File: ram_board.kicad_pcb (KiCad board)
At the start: 2 copper layers, 73 x 31.6 mm, 20 parts, among them J1 Conn_02x20_Odd_Even, J2 Conn_02x05_Odd_Even, U1 IS61LV5128AL-10TLI, U2 SST39VF040-70-4C-NHE, U3 74LVC04A

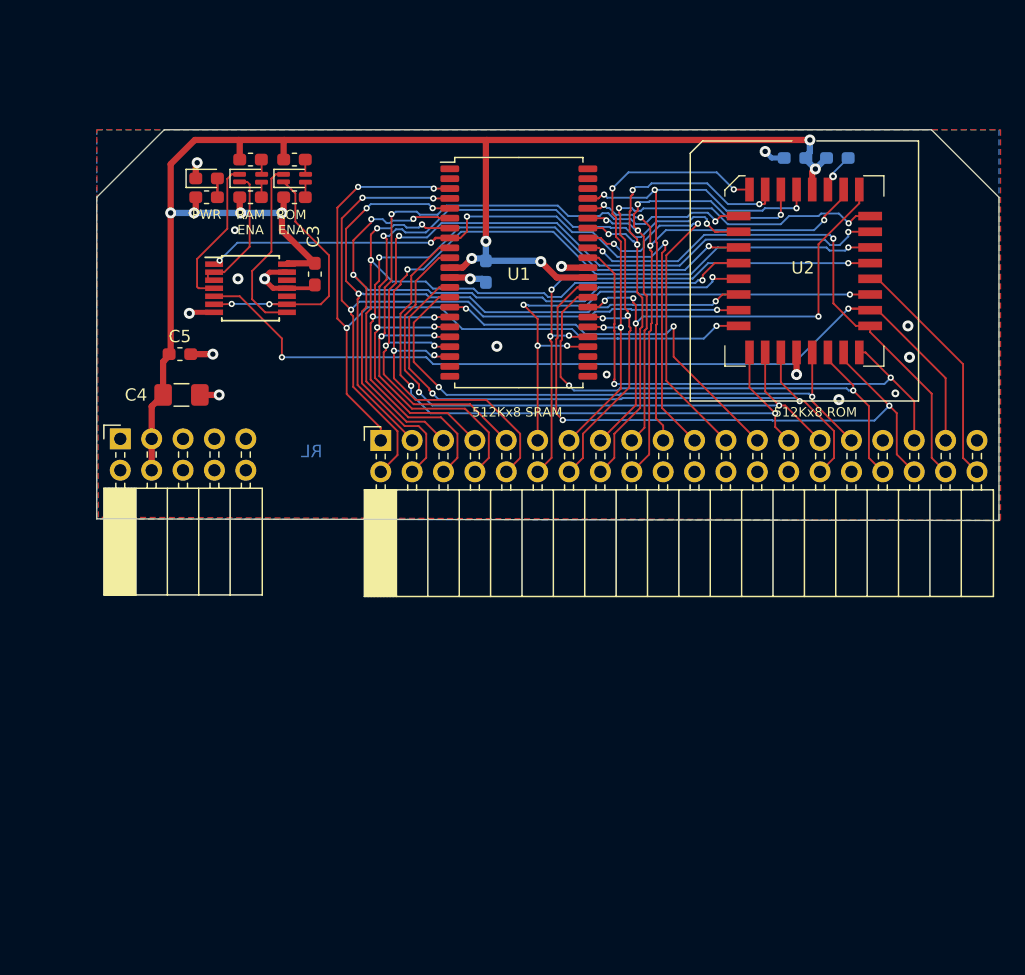
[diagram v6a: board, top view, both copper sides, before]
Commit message: fixed leds, spacing
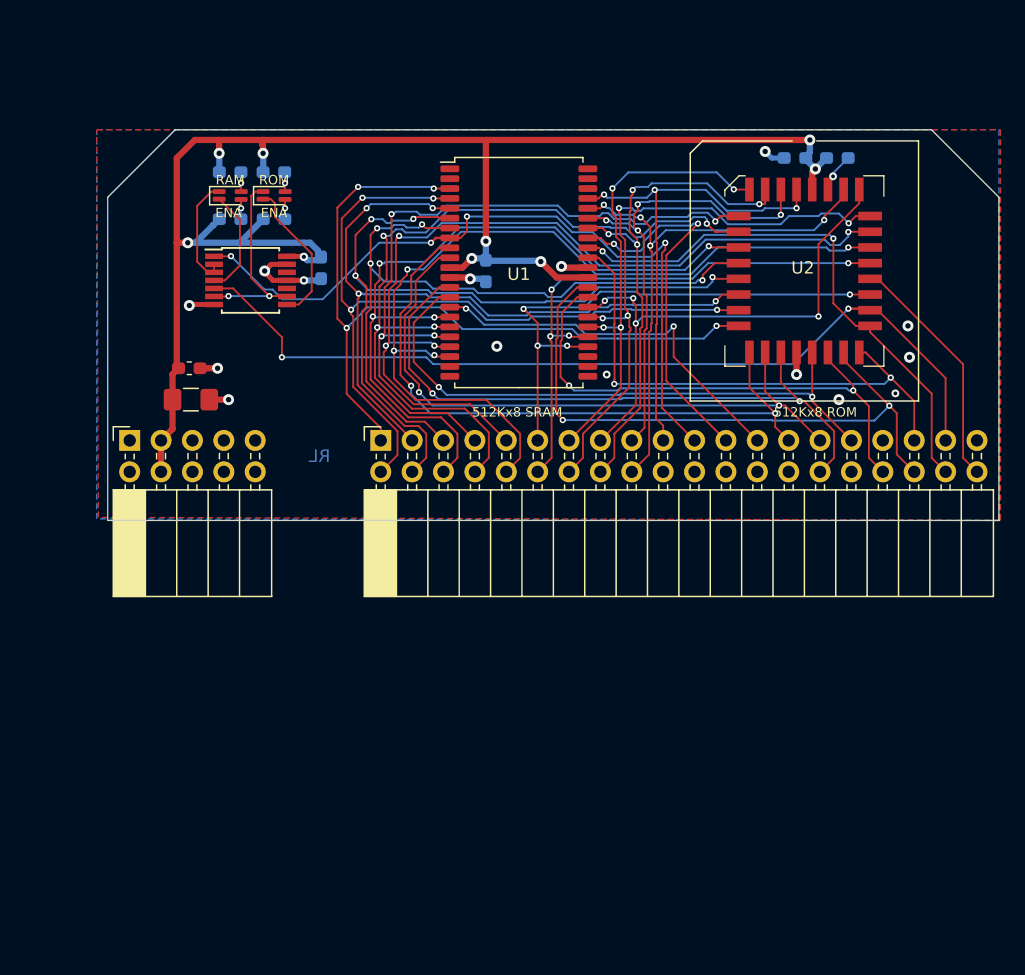
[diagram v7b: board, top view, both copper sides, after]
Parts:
- removed D1: LED, LED_SMD:LED_0603_1608Metric_Pad1.05x0.95mm_HandSolder
- removed R1: 360R, Resistor_SMD:R_0603_1608Metric_Pad1.05x0.95mm_HandSolder
- C3, R3, R4, R5, R6: moved to B.Cu
- moved G*** 33.7 mm to (167.4, 86.1)
- moved R6 5.10 mm to (131.4, 79.8)
- moved R4 5.10 mm to (127.9, 79.8)
- moved R5 2.63 mm to (131.4, 75.9)
- moved R3 2.62 mm to (127.9, 75.9)
- moved D3 2.16 mm to (131.4, 77.9)
- moved D2 2.16 mm to (127.9, 77.9)
- moved C5 1.37 mm to (124.6, 91.8)
- moved C4 0.85 mm to (124.7, 94.4)
- moved J2 0.77 mm to (119.8, 97.7)
- moved C3 0.72 mm to (135.3, 83.7)
- moved U3 0.63 mm to (129.5, 84.7)
- moved C2 0.05 mm to (148.6, 83.9)
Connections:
- R3 pad 1: Net-(D2-Pad3) -> Net-(D2-Pad1)
- R4 pad 1: Net-(D2-Pad1) -> Net-(D2-Pad3)
- R5 pad 1: Net-(D3-Pad3) -> Net-(D3-Pad1)
- R6 pad 1: Net-(D3-Pad1) -> Net-(D3-Pad3)
- U3 pad 2: Net-(D2-Pad4) -> Net-(D2-Pad2)
- U3 pad 3: Net-(D2-Pad4) -> Net-(D2-Pad2)
- U3 pad 4: Net-(D2-Pad2) -> Net-(D2-Pad4)
- U3 pad 6: Net-(D3-Pad4) -> Net-(D3-Pad2)
- U3 pad 8: Net-(D3-Pad2) -> Net-(D3-Pad4)
- U3 pad 9: Net-(D3-Pad4) -> Net-(D3-Pad2)
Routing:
- net Net-(D3-Pad4): track 22.2 -> 11.9 mm, vias 2 -> 0
- net /RAM_CE: track 58.4 -> 61.2 mm
- net Net-(D2-Pad2): track 11.8 -> 9.15 mm
- net +3V3: track 130.9 -> 133.4 mm
- net Net-(D2-Pad4): track 10.8 -> 8.85 mm
- net Net-(D3-Pad2): track 15.3 -> 17.2 mm, vias 0 -> 2
- net Net-(D1-Pad2): track 1.52 -> 0.00 mm
- net GND: track 23.5 -> 22.0 mm, vias 17 -> 15
- net Net-(D3-Pad1): track 1.20 -> 1.62 mm, vias 0 -> 1
- net Net-(D3-Pad3): track 1.22 -> 1.61 mm, vias 0 -> 1
- net Net-(D2-Pad3): track 1.22 -> 1.61 mm, vias 0 -> 1
- net Net-(D2-Pad1): track 1.20 -> 1.59 mm, vias 0 -> 1
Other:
- board size 73 x 31.6 mm -> 72.1 x 31.6 mm
- board text added: "DeltaBrd RAM/ROM Extension v1.0 © 2019 by Hyiger Designs"
- board text added: "ENA"
- board text added: "RAM"
- board text added: "ROM"
- board text removed: "DeltaBrd RAM/ROM Extension v1.0 © 2019 by Hyiger Designs DeltaBrd © Dr. Svetozar Ilchev http://ilchev.net/deltabrd"
- board text removed: "PWR"
- board text removed: "RAM ENA"
- board text removed: "ROM ENA"

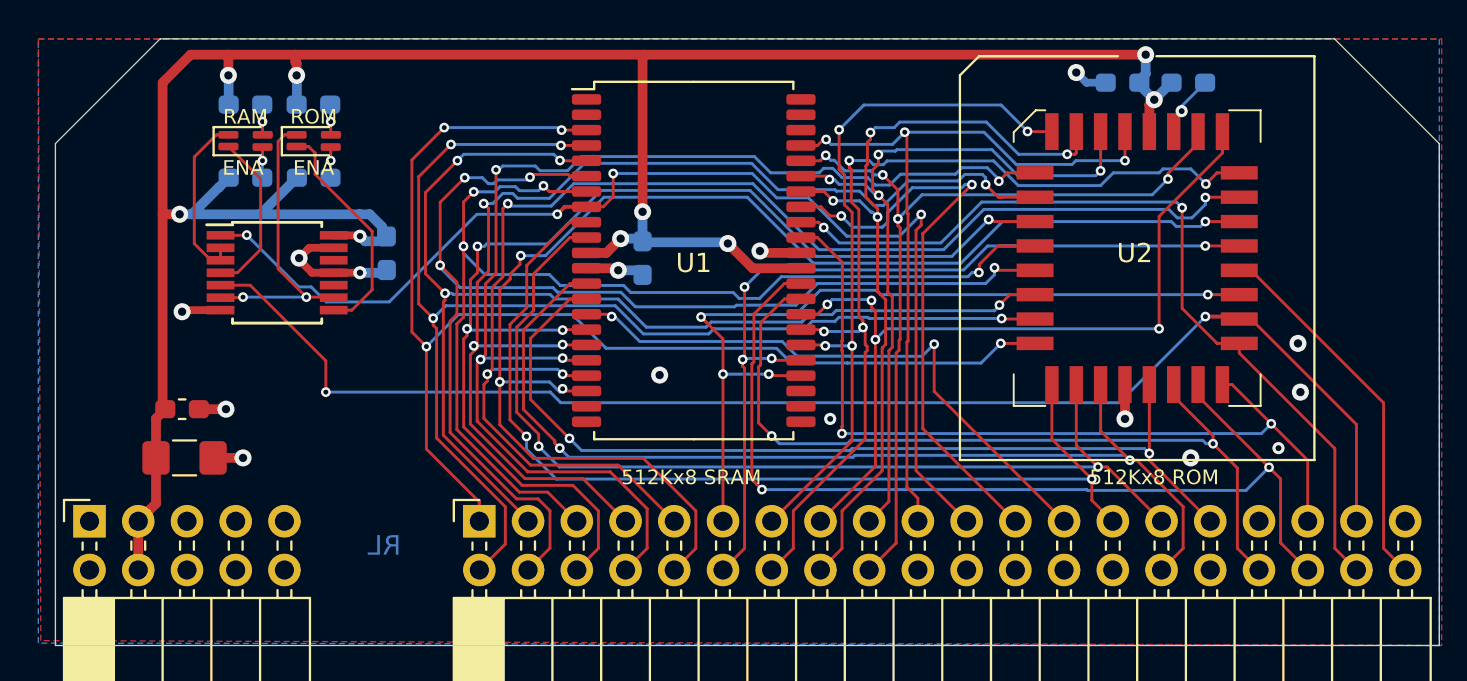
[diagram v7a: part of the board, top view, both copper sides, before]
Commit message: gnd plane stitching
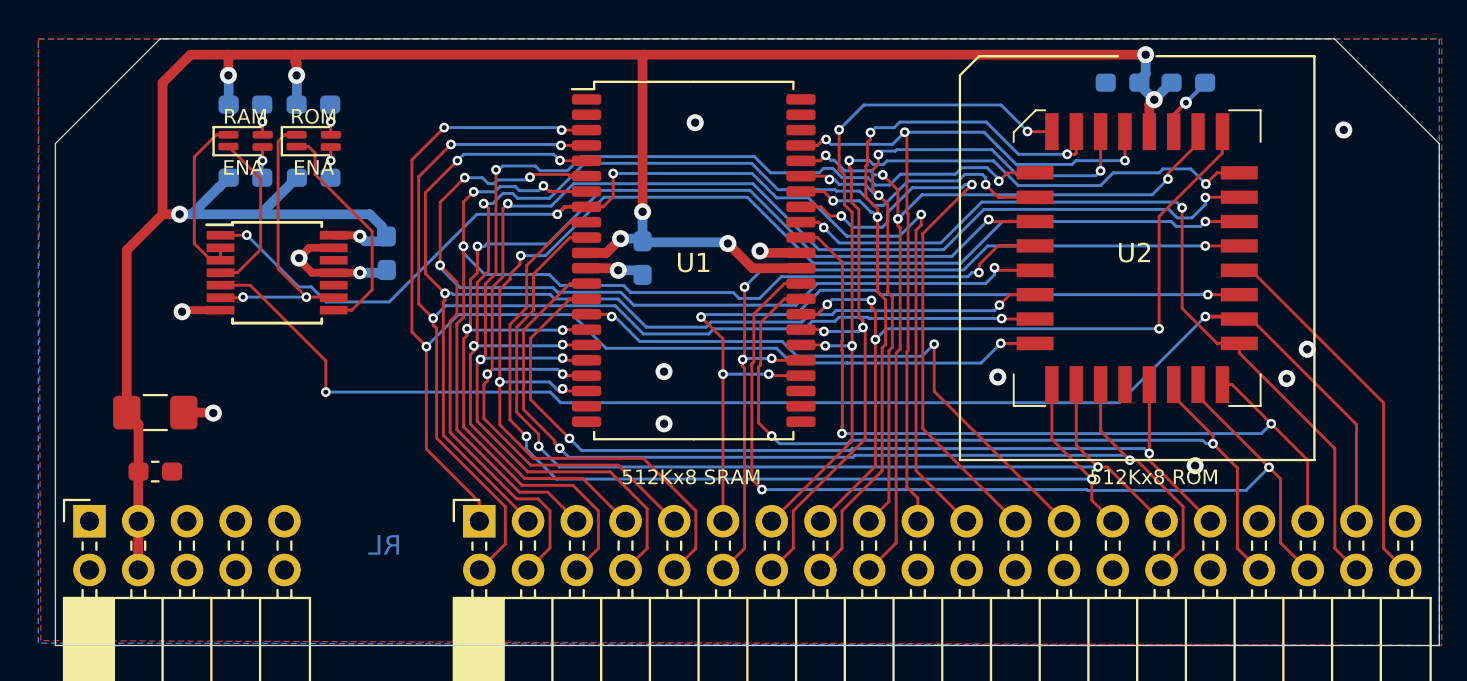
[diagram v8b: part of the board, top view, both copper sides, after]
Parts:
- moved C5 3.54 mm to (123.2, 95.1)
- moved C4 2.81 mm to (123.2, 92.0)
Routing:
- net GND: track 22.0 -> 17.2 mm, vias 15 -> 14
- net Net-(R2-Pad1): track 3.23 -> 4.02 mm
